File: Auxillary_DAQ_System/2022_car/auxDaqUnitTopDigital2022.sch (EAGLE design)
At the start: 44 parts

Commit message: Completed auxDAQ rev1
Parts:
- removed A0, A1, A10, A11, A12, A13, A14, A15, A16, A17, A18, A19, A2, A20, A21, A22, A23, A3, A4, A5, A6, A7, A8, A9: (no value), GTOR - Microfit Connector:HEADER_POS3_43650-0300
- removed JP1: (no value), GTOR - Connectors:PINHD-1X24
- removed JP4, JP5, JP6: (no value), GTOR - Connectors:PINHD-1X8
- added CS=1, CS=2: (no value), GTOR - Microfit Connector:HEADER_POS6_43045-0600
- added D10, D11, D12, D7, D8, D9: (no value), GTOR - Microfit Connector:HEADER_POS3_43650-0300
- added I2C3, I2C4: (no value), GTOR - Microfit Connector:HEADER_POS4_43045-0401
- JP2: device GTOR - Connectors:PINHD-1X24 -> GTOR - Connectors:PINHD-1X22
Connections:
- removed net 0: JP1.2
- removed net 1: JP1.3
- removed net 10: JP1.12
- removed net 22: JP2.5
- removed net 23: JP2.4
- removed net 33: JP2.24, R1.1
- removed net 34: JP2.23
- removed net 35: JP2.22
- removed net 36: JP2.21
- removed net 37: JP2.20
- removed net 38: JP2.19
- removed net 39: JP2.18
- removed net 3V3-1: JP1.15
- removed net 3V3-3: JP2.3
- removed net 40: JP2.17
- removed net 41: JP2.16
- removed net A0: JP2.13
- removed net A1: JP2.12
- removed net A2: JP2.11
- removed net A3: JP2.10
- removed net A6: JP2.7
- removed net A7: JP2.6
- removed net ADC1: A0.2, JP6.1
- removed net ADC10: A9.2, JP5.2
- removed net ADC11: A10.2, JP5.3
- removed net ADC12: A11.2, JP5.4
- removed net ADC13: A12.2, JP5.5
- removed net ADC14: A13.2, JP5.6
- removed net ADC15: A14.2, JP5.7
- removed net ADC16: A15.2, JP5.8
- removed net ADC17: A16.2, JP4.1
- removed net ADC18: A17.2, JP4.2
- removed net ADC19: A18.2, JP4.3
- removed net ADC2: A1.2, JP6.2
- removed net ADC20: A19.2, JP4.4
- removed net ADC21: A20.2, JP4.5
- removed net ADC22: A21.2, JP4.6
- removed net ADC23: A22.2, JP4.7
- removed net ADC24: A23.2, JP4.8
- removed net ADC3: A2.2, JP6.3
- removed net ADC4: A3.2, JP6.4
- removed net ADC5: A4.2, JP6.5
- removed net ADC6: A5.2, JP6.6
- removed net ADC7: A6.2, JP6.7
- removed net ADC8: A7.2, JP6.8
- removed net ADC9: A8.2, JP5.1
- removed net GND1: JP1.1
- removed net VIN: JP2.1
- net +3V3: now also CS=1.1, CS=2.1, D10.1, D11.1, D12.1, D7.1, D8.1, D9.1, I2C3.1, I2C4.1
- net +5V: no longer A0.1, A1.1, A10.1, A11.1, A12.1, A13.1, A14.1, A15.1, A16.1, A17.1, A18.1, A19.1, A2.1, A20.1, A21.1, A22.1, A23.1, A3.1, A4.1, A5.1, A6.1, A7.1, A8.1, A9.1
- net 2: now also JP2.2; no longer JP1.4
- net 24: now also CS=1.2, JP2.16; no longer JP1.16
- net 25: now also CS=2.2, JP2.17; no longer JP1.17
- net 26: now also D7.2, JP2.8; no longer JP1.18
- net 27: now also D8.2, JP2.9; no longer JP1.19
- net 28: now also D9.2, JP2.10; no longer JP1.20
- net 29: now also D10.2, JP2.11; no longer JP1.21
- net 3: now also JP2.3; no longer JP1.5
- net 30: now also JP2.1, R1.1; no longer JP1.22
- net 31: now also D11.2, JP2.12; no longer JP1.23
- net 32: now also D12.2, JP2.13; no longer JP1.24
- net 4: now also JP2.4; no longer JP1.6
- net 5: now also JP2.5; no longer JP1.7
- net 6: now also JP2.6; no longer JP1.8
- net 7: now also JP2.7; no longer JP1.9
- net 8: now also JP2.14; no longer JP1.10
- net 9: now also JP2.15; no longer JP1.11
- net GND: now also CS=1.6, CS=2.6, D10.3, D11.3, D12.3, D7.3, D8.3, D9.3, I2C3.4, I2C4.4; no longer A0.3, A1.3, A10.3, A11.3, A12.3, A13.3, A14.3, A15.3, A16.3, A17.3, A18.3, A19.3, A2.3, A20.3, A21.3, A22.3, A23.3, A3.3, A4.3, A5.3, A6.3, A7.3, A8.3, A9.3, JP2.15, JP2.2
- net MISO: now also CS=1.4, CS=2.4, JP2.20; no longer JP1.14
- net MOSI: now also CS=1.3, CS=2.3, JP2.19; no longer JP1.13
- net SCK: now also CS=1.5, CS=2.5, JP2.18; no longer JP2.14
- net SCL: now also I2C3.3, I2C4.3, JP2.21; no longer JP2.8
- net SDA: now also I2C3.2, I2C4.2, JP2.22; no longer JP2.9
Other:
- note removed: "Analog Pins"
- moved on the sheet: D1, D2, D3, D4, D5, D6, JP3

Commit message: Minor DRC fixes and trace thickening
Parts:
- removed JP3: (no value), GTOR - Connectors:PINHD-1X3
- added JP1: (no value), GTOR - Connectors:PINHD-1X2
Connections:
- removed net +5V: JP3.3
- net +3V3: now also JP1.2; no longer JP3.2
- net GND: now also JP1.1; no longer JP3.1
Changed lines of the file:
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@@
 <attribute name="NAMEYEAR" value="PETER2022"/>
 </part>
-<part name="JP3" library="GTOR - Connectors" deviceset="PINHD-1X3" device="" package3d_urn="urn:adsk.eagle:package:22458/2"/>
-<part name="P+4" library="GTOR - Documation Frame" deviceset="+5V" device=""/>
 <part name="+3V2" library="GTOR - Documation Frame" deviceset="+3V3" device=""/>
 <part name="SUPPLY4" library="GTOR - Documation Frame" deviceset="GND" device=""/>
@@
 <part name="SUPPLY20" library="GTOR - Documation Frame" deviceset="GND" device=""/>
 <part name="JP2" library="GTOR - Connectors" deviceset="PINHD-1X22" device="" package3d_urn="urn:adsk.eagle:package:22442/3"/>
+<part name="JP1" library="GTOR - Connectors" deviceset="PINHD-1X2" device="" package3d_urn="urn:adsk.eagle:package:22435/2"/>
 </parts>
 <sheets>
@@
 <attribute name="NAMEYEAR" x="147.32" y="0" size="1.27" layer="96" display="off"/>
 </instance>
-<instance part="JP3" gate="A" x="215.9" y="160.02" smashed="yes" rot="R180">
-<attribute name="NAME" x="222.25" y="154.305" size="1.778" layer="95" rot="R180"/>
-<attribute name="VALUE" x="222.25" y="167.64" size="1.778" layer="96" rot="R180"/>
-</instance>
-<instance part="P+4" gate="1" x="226.06" y="170.18" smashed="yes">
-<attribute name="VALUE" x="233.68" y="170.18" size="1.778" layer="96" rot="R180"/>
-</instance>
 <instance part="+3V2" gate="G$1" x="228.6" y="165.1" smashed="yes">
 <attribute name="VALUE" x="236.22" y="165.1" size="1.778" layer="96" rot="R180"/>
@@
 <attribute name="NAME" x="222.25" y="83.185" size="1.778" layer="95" rot="R180"/>
 <attribute name="VALUE" x="222.25" y="144.78" size="1.778" layer="96" rot="R180"/>
+</instance>
+<instance part="JP1" gate="G$1" x="215.9" y="160.02" smashed="yes" rot="R180">
+<attribute name="NAME" x="222.25" y="154.305" size="1.778" layer="95" rot="R180"/>
+<attribute name="VALUE" x="222.25" y="165.1" size="1.778" layer="96" rot="R180"/>
 </instance>
 </instances>
@@
 <net name="GND" class="0">
 <segment>
-<pinref part="JP3" gate="A" pin="1"/>
 <pinref part="SUPPLY4" gate="GND" pin="GND"/>
 <wire x1="218.44" y1="157.48" x2="226.06" y2="157.48" width="0.1524" layer="91"/>
 <wire x1="226.06" y1="157.48" x2="226.06" y2="154.94" width="0.1524" layer="91"/>
+<pinref part="JP1" gate="G$1" pin="1"/>
 </segment>
 <segment>
@@
 </segment>
 </net>
-<net name="+5V" class="0">
-<segment>
-<pinref part="JP3" gate="A" pin="3"/>
-<pinref part="P+4" gate="1" pin="+5V"/>
-<wire x1="218.44" y1="162.56" x2="226.06" y2="162.56" width="0.1524" layer="91"/>
-<wire x1="226.06" y1="162.56" x2="226.06" y2="167.64" width="0.1524" layer="91"/>
-</segment>
-</net>
 <net name="+3V3" class="0">
 <segment>
-<pinref part="JP3" gate="A" pin="2"/>
 <pinref part="+3V2" gate="G$1" pin="+3V3"/>
 <wire x1="218.44" y1="160.02" x2="228.6" y2="160.02" width="0.1524" layer="91"/>
 <wire x1="228.6" y1="160.02" x2="228.6" y2="162.56" width="0.1524" layer="91"/>
-</segment>
-<segment>
+<pinref part="JP1" gate="G$1" pin="2"/>
+</segment>
+<segment>

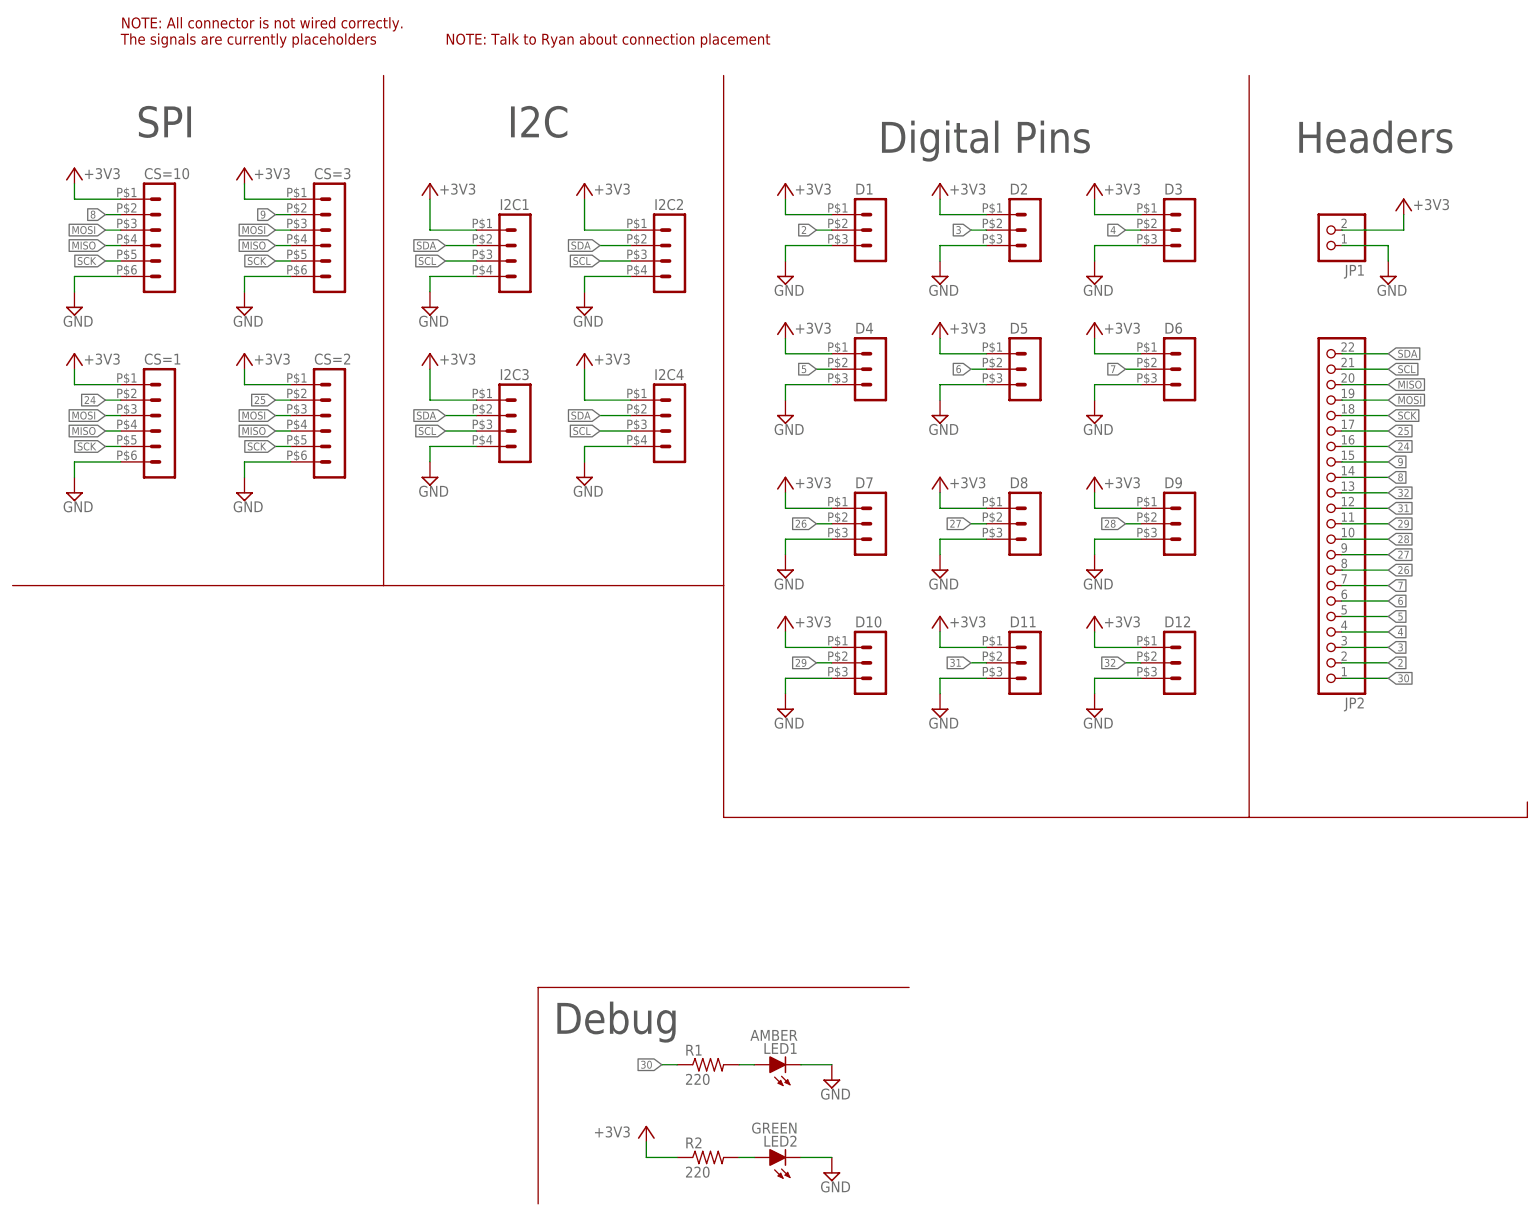
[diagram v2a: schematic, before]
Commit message: Bottom board has some airwires, but everything should line up
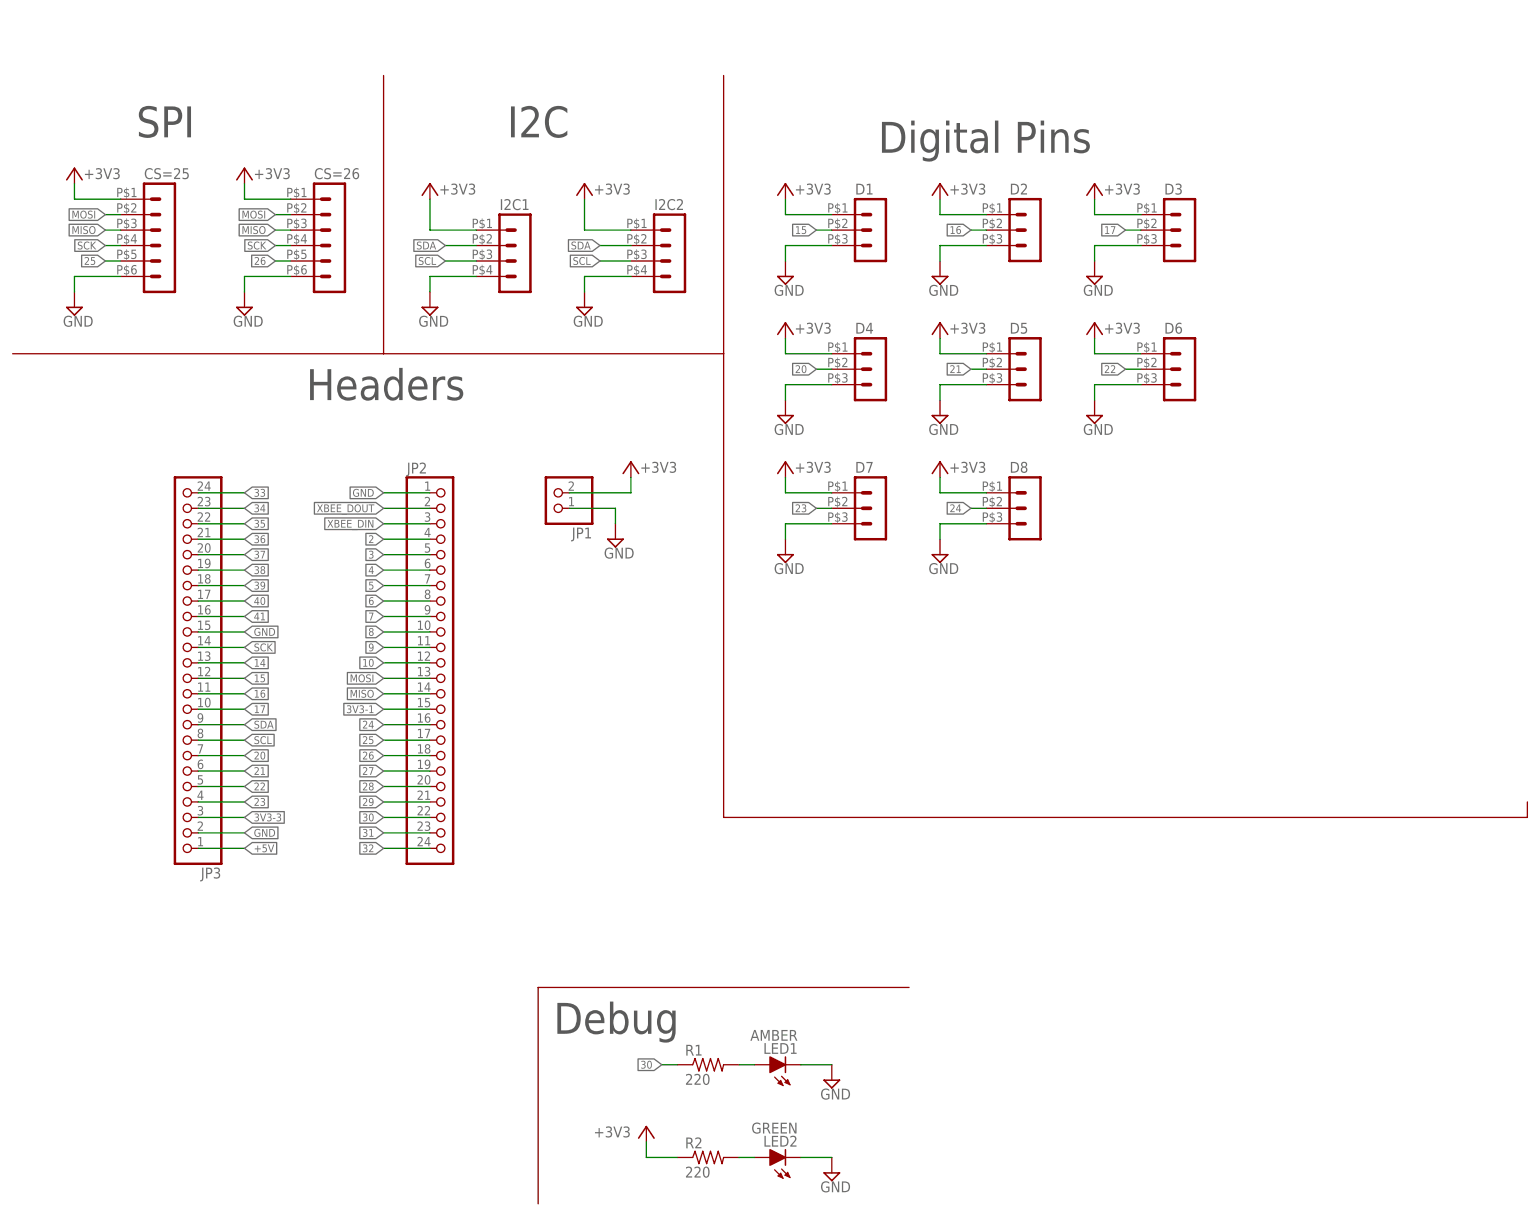
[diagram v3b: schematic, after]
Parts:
- removed CS=1, CS=2: (no value), GTOR - Microfit Connector:HEADER_POS6_43045-0600
- removed D10, D11, D12, D9: (no value), GTOR - Microfit Connector:HEADER_POS3_43650-0300
- removed I2C3, I2C4: (no value), GTOR - Microfit Connector:HEADER_POS4_43045-0401
- added JP3: (no value), GTOR - Connectors:PINHD-1X24
- JP2: device GTOR - Connectors:PINHD-1X22 -> GTOR - Connectors:PINHD-1X24
- renumbered CS=10 to CS=25, CS=3 to CS=26
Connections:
- new net +5V: JP3.1
- new net 10: JP2.12
- new net 14: JP3.13
- new net 15: D1.2, JP3.12
- new net 16: D2.2, JP3.11
- new net 17: D3.2, JP3.10
- new net 20: D4.2, JP3.7
- new net 21: D5.2, JP3.6
- new net 22: D6.2, JP3.5
- new net 23: D7.2, JP3.4
- new net 33: JP3.24
- new net 34: JP3.23
- new net 35: JP3.22
- new net 36: JP3.21
- new net 37: JP3.20
- new net 38: JP3.19
- new net 39: JP3.18
- new net 3V3-1: JP2.15
- new net 3V3-3: JP3.3
- new net 40: JP3.17
- new net 41: JP3.16
- new net XBEE_DIN: JP2.3
- new net XBEE_DOUT: JP2.2
- net +3V3: no longer CS=1.1, CS=2.1, D10.1, D11.1, D12.1, D9.1, I2C3.1, I2C4.1
- net 2: now also JP2.4; no longer D1.2, JP2.2
- net 24: now also D8.2; no longer CS=1.2
- net 25: now also CS=25.5; no longer CS=2.2
- net 26: now also CS=26.5, JP2.18; no longer D7.2, JP2.8
- net 27: now also JP2.19; no longer D8.2, JP2.9
- net 28: now also JP2.20; no longer D9.2, JP2.10
- net 29: now also JP2.21; no longer D10.2, JP2.11
- net 3: now also JP2.5; no longer D2.2, JP2.3
- net 30: now also JP2.22; no longer JP2.1
- net 31: now also JP2.23; no longer D11.2, JP2.12
- net 32: now also JP2.24; no longer D12.2, JP2.13
- net 4: now also JP2.6; no longer D3.2, JP2.4
- net 5: now also JP2.7; no longer D4.2, JP2.5
- net 6: now also JP2.8; no longer D5.2, JP2.6
- net 7: now also JP2.9; no longer D6.2, JP2.7
- net 8: now also JP2.10; no longer CS=25.2, JP2.14
- net 9: now also JP2.11; no longer CS=26.2, JP2.15
- net GND: now also JP2.1, JP3.15, JP3.2; no longer CS=1.6, CS=2.6, D10.3, D11.3, D12.3, D9.3, I2C3.4, I2C4.4
- net MISO: now also CS=25.3, CS=26.3, JP2.14; no longer CS=1.4, CS=2.4, CS=25.4, CS=26.4, JP2.20
- net MOSI: now also CS=25.2, CS=26.2, JP2.13; no longer CS=1.3, CS=2.3, CS=25.3, CS=26.3, JP2.19
- net SCK: now also CS=25.4, CS=26.4, JP3.14; no longer CS=1.5, CS=2.5, CS=25.5, CS=26.5, JP2.18
- net SCL: now also JP3.8; no longer I2C3.3, I2C4.3, JP2.21
- net SDA: now also JP3.9; no longer I2C3.2, I2C4.2, JP2.22
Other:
- note removed: "NOTE: All connector is not wired correctly. The signals are currently placeholders"
- note removed: "NOTE: Talk to Ryan about connection placement"
- moved on the sheet: D7, D8, JP1

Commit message: Started changes for new Aux Daq
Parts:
- removed JP1: (no value), GTOR - Connectors:PINHD-1X2
- removed JP2, JP3: (no value), GTOR - Connectors:PINHD-1X24
- added JP10, JP7: (no value), GTOR - Connectors:PINHD-1X24
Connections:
- removed net 3V3-3: JP3.3
- net +3V3: now also JP10.3; no longer JP1.2
- net +5V: now also JP10.1; no longer JP3.1
- net 10: now also JP7.12; no longer JP2.12
- net 14: now also JP10.13; no longer JP3.13
- net 15: now also JP10.12; no longer JP3.12
- net 16: now also JP10.11; no longer JP3.11
- net 17: now also JP10.10; no longer JP3.10
- net 2: now also JP7.4; no longer JP2.4
- net 20: now also JP10.7; no longer JP3.7
- net 21: now also JP10.6; no longer JP3.6
- net 22: now also JP10.5; no longer JP3.5
- net 23: now also JP10.4; no longer JP3.4
- net 24: now also JP7.16; no longer JP2.16
- net 25: now also JP7.17; no longer JP2.17
- net 26: now also JP7.18; no longer JP2.18
- net 27: now also JP7.19; no longer JP2.19
- net 28: now also JP7.20; no longer JP2.20
- net 29: now also JP7.21; no longer JP2.21
- net 3: now also JP7.5; no longer JP2.5
- net 30: now also JP7.22; no longer JP2.22
- net 31: now also JP7.23; no longer JP2.23
- net 32: now also JP7.24; no longer JP2.24
- net 33: now also JP10.24; no longer JP3.24
- net 34: now also JP10.23; no longer JP3.23
- net 35: now also JP10.22; no longer JP3.22
- net 36: now also JP10.21; no longer JP3.21
- net 37: now also JP10.20; no longer JP3.20
- net 38: now also JP10.19; no longer JP3.19
- net 39: now also JP10.18; no longer JP3.18
- net 3V3-1: now also JP7.15; no longer JP2.15
- net 4: now also JP7.6; no longer JP2.6
- net 40: now also JP10.17; no longer JP3.17
- net 41: now also JP10.16; no longer JP3.16
- net 5: now also JP7.7; no longer JP2.7
- net 6: now also JP7.8; no longer JP2.8
- net 7: now also JP7.9; no longer JP2.9
- net 8: now also JP7.10; no longer JP2.10
- net 9: now also JP7.11; no longer JP2.11
- net GND: now also JP10.15, JP10.2, JP7.1; no longer JP1.1, JP2.1, JP3.15, JP3.2
- net MISO: now also JP7.14; no longer JP2.14
- net MOSI: now also JP7.13; no longer JP2.13
- net SCK: now also JP10.14; no longer JP3.14
- net SCL: now also JP10.8; no longer JP3.8
- net SDA: now also JP10.9; no longer JP3.9
- net XBEE_DIN: now also JP7.3; no longer JP2.3
- net XBEE_DOUT: now also JP7.2; no longer JP2.2
